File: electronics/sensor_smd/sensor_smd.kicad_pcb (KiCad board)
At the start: 2 copper layers, 40 x 20 mm, 7 parts, among them J1 HEADER MALE RA, U1 HX6286

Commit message: Updates
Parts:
- JP1: moved to B.Cu
- moved JP1 8.40 mm to (129.9, 95.0), turned to 0 degrees
- moved D1 3.50 mm to (131.0, 100.0)
- moved R1 3.00 mm to (128.0, 100.0), turned to 90 degrees
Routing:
- net Net-(R1-Pad2): track 15.8 -> 6.09 mm, vias 0 -> 1
- net VDD: track 20.3 -> 27.9 mm, vias 0 -> 1
- net /SIGNAL: track 14.6 -> 16.8 mm
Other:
- board text added: "↑ Cut to disable LED"
- board text removed: "Cut to disable LED"

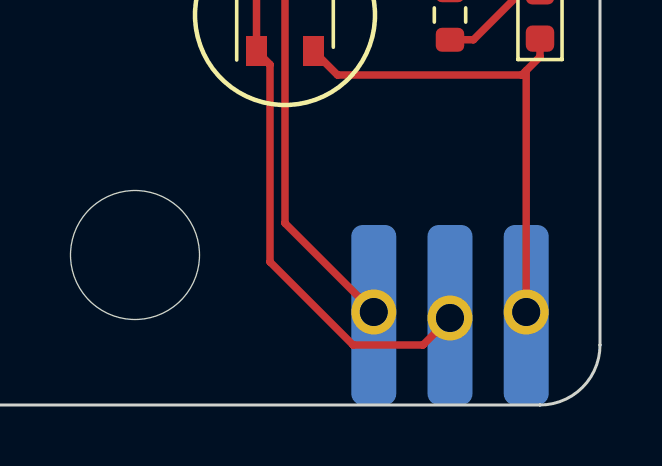
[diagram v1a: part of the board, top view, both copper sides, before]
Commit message: Remove SMD pads from header footprint
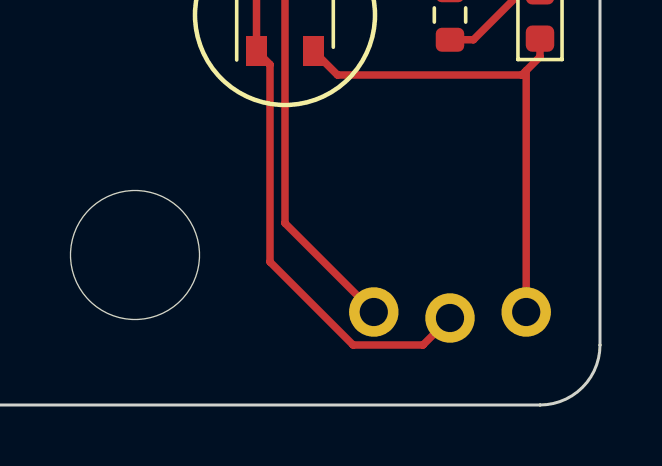
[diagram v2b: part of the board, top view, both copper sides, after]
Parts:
- J1: footprint sensor_smd_lib:header_3_smd -> sensor_smd_lib:header_3
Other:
- board text added: "${COMMIT_HASH} ${COMMIT_DATE}"
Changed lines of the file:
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@@
     )
   )
+  (property "COMMIT_DATE" "YYYY-MM-DD")
+  (property "COMMIT_HASH" "deadbeef")
   (net 0 "")
   (net 1 "/SIGNAL")
@@
     )
   )
-  (footprint "sensor_smd_lib:header_3_smd" (layer "B.Cu")
+  (footprint "sensor_smd_lib:header_3" (layer "B.Cu")
     (at 128 113 180)
     (property "Sheetfile" "sensor_smd.kicad_sch")
     (property "Sheetname" "")
-    (attr smd)
+    (attr through_hole exclude_from_pos_files)
     (fp_text reference "J1" (at 0 0.5 unlocked) (layer "B.SilkS") hide
       (effects (font (size 1 1) (thickness 0.15)) (justify mirror))
@@
       (effects (font (size 1 1) (thickness 0.15)) (justify mirror))
     )
-    (fp_line (start -4 6.5) (end 4 6.5) (layer "B.SilkS") (width 0.12))
-    (fp_line (start 4 6.5) (end 4 0) (layer "B.SilkS") (width 0.12))
-    (fp_line (start -4 0) (end -4 6.5) (layer "B.SilkS") (width 0.12))
+    (fp_line (start 4 4.5) (end 4 0) (layer "B.SilkS") (width 0.12))
+    (fp_line (start -4 0) (end -4 4.5) (layer "B.SilkS") (width 0.12))
+    (fp_line (start -4 4.5) (end 4 4.5) (layer "B.SilkS") (width 0.12))
     (fp_line (start -4 -12) (end 4 -12) (layer "B.Fab") (width 0.1))
     (fp_line (start 4 -12) (end 4 0) (layer "B.Fab") (width 0.1))
     (fp_line (start -4 0) (end -4 -12) (layer "B.Fab") (width 0.1))
-    (pad "1" thru_hole circle (at -2.54 3.1 180) (size 1.5 1.5) (drill 0.94) (layers *.Cu *.Mask)
+    (pad "1" thru_hole circle (at -2.54 3.1 180) (size 1.65 1.65) (drill 0.94) (layers *.Cu *.Mask)
       (net 1 "/SIGNAL") (pinfunction "Pin_1") (pintype "passive"))
-    (pad "1" smd roundrect (at -2.54 3 180) (size 1.5 6) (layers "B.Cu" "B.Paste" "B.Mask") (roundrect_rratio 0.25)
-      (net 1 "/SIGNAL") (pinfunction "Pin_1") (pintype "passive"))
-    (pad "2" thru_hole circle (at 0 2.9 180) (size 1.5 1.5) (drill 0.94) (layers *.Cu *.Mask)
+    (pad "2" thru_hole circle (at 0 2.9 180) (size 1.65 1.65) (drill 0.94) (layers *.Cu *.Mask)
       (net 3 "VDD") (pinfunction "Pin_2") (pintype "passive"))
-    (pad "2" smd roundrect (at 0 3 180) (size 1.5 6) (layers "B.Cu" "B.Paste" "B.Mask") (roundrect_rratio 0.25)
-      (net 3 "VDD") (pinfunction "Pin_2") (pintype "passive"))
-    (pad "3" thru_hole circle (at 2.54 3.1 180) (size 1.5 1.5) (drill 0.94) (layers *.Cu *.Mask)
+    (pad "3" thru_hole circle (at 2.54 3.1 180) (size 1.65 1.65) (drill 0.94) (layers *.Cu *.Mask)
       (net 4 "GND") (pinfunction "Pin_3") (pintype "passive"))
-    (pad "3" smd roundrect (at 2.54 3 180) (size 1.5 6) (layers "B.Cu" "B.Paste" "B.Mask") (roundrect_rratio 0.25)
-      (net 4 "GND") (pinfunction "Pin_3") (pintype "passive"))
-    (model "${KICAD6_3DMODEL_DIR}/Connector_PinHeader_2.54mm.3dshapes/PinHeader_1x03_P2.54mm_Vertical.step"
+    (model "${KICAD6_3DMODEL_DIR}/Connector_PinHeader_2.54mm.3dshapes/PinHeader_1x03_P2.54mm_Vertical.step" hide
       (offset (xyz -2.54 0 0.3))
       (scale (xyz 1 1 1))
       (rotate (xyz -90 90 0))
+    )
+    (model "${KICAD6_3DMODEL_DIR}/Connector_PinHeader_2.54mm.3dshapes/PinHeader_1x03_P2.54mm_Horizontal.step"
+      (offset (xyz 2.54 3 0))
+      (scale (xyz 1 1 1))
+      (rotate (xyz 0 0 90))
     )
   )
@@
   (gr_arc (start 131 93) (mid 132.414214 93.585786) (end 133 95) (layer "Edge.Cuts") (width 0.1))
   (gr_arc (start 95 113) (mid 93.585786 112.414214) (end 93 111) (layer "Edge.Cuts") (width 0.1))
-  (gr_text "S" (at 130.5 105.5) (layer "B.SilkS")
+  (gr_text "S" (at 130.5 107.5) (layer "B.SilkS")
     (effects (font (size 1 1) (thickness 0.15)) (justify mirror))
   )
-  (gr_text "MOTOR" (at 102 109 -10) (layer "B.SilkS")
+  (gr_text "MOTOR" (at 102 107 15) (layer "B.SilkS")
     (effects (font (size 3 3) (thickness 0.3)) (justify mirror))
   )
-  (gr_text "-" (at 125.5 105.5) (layer "B.SilkS")
+  (gr_text "${COMMIT_HASH}\n${COMMIT_DATE}" (at 112.5 110.5) (layer "B.SilkS")
+    (effects (font (size 1 1) (thickness 0.15)) (justify left mirror))
+  )
+  (gr_text "-" (at 125.5 107.5) (layer "B.SilkS")
     (effects (font (size 1 1) (thickness 0.15)) (justify mirror))
   )
-  (gr_text "+" (at 128 105.5) (layer "B.SilkS")
+  (gr_text "+" (at 128 107.5) (layer "B.SilkS")
     (effects (font (size 1 1) (thickness 0.15)) (justify mirror))
   )

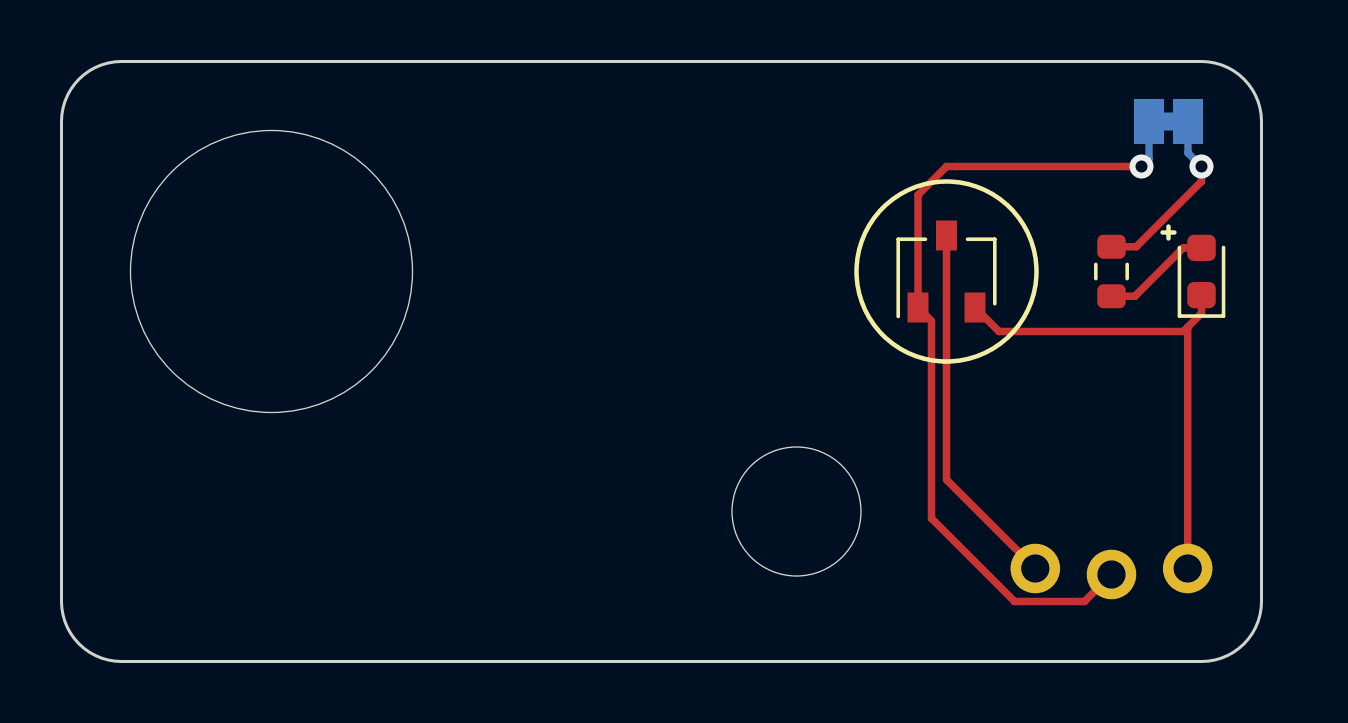
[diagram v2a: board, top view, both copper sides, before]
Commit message: Fix clearance
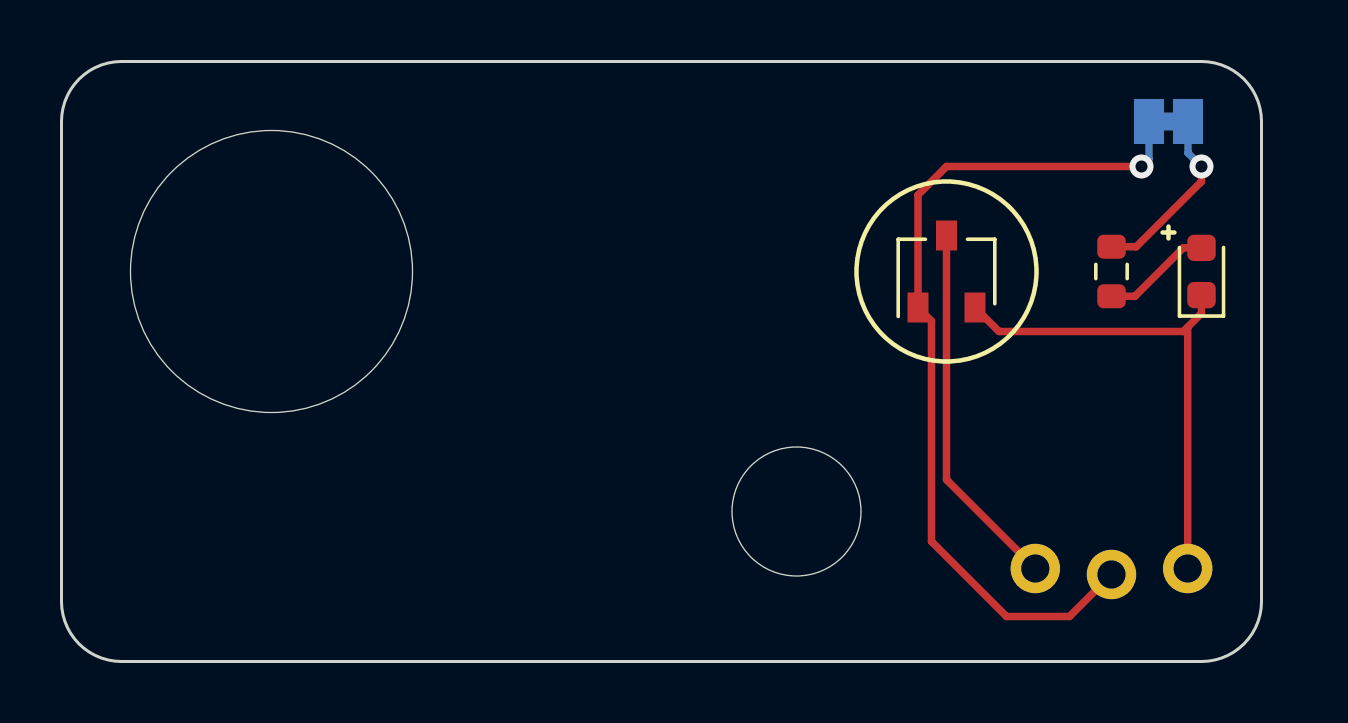
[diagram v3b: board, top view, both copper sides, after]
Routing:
- net VDD: track 27.9 -> 28.8 mm
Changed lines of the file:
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@@
   (segment (start 130.39375 99.2125) (end 131 99.2125) (width 0.25) (layer "F.Cu") (net 2))
   (segment (start 128 100.825) (end 128.78125 100.825) (width 0.25) (layer "F.Cu") (net 2))
-  (segment (start 127.1 111) (end 128 110.1) (width 0.25) (layer "F.Cu") (net 3))
-  (segment (start 122 108.23014) (end 124.76986 111) (width 0.25) (layer "F.Cu") (net 3))
   (segment (start 122.5 96.5) (end 129 96.5) (width 0.25) (layer "F.Cu") (net 3))
+  (segment (start 122 101.65) (end 122 109) (width 0.25) (layer "F.Cu") (net 3))
+  (segment (start 126.6 111.5) (end 128 110.1) (width 0.25) (layer "F.Cu") (net 3))
+  (segment (start 121.55 97.45) (end 122.5 96.5) (width 0.25) (layer "F.Cu") (net 3))
+  (segment (start 124.5 111.5) (end 126.6 111.5) (width 0.25) (layer "F.Cu") (net 3))
+  (segment (start 121.55 101.2) (end 121.55 97.45) (width 0.25) (layer "F.Cu") (net 3))
   (segment (start 121.55 101.2) (end 122 101.65) (width 0.25) (layer "F.Cu") (net 3))
-  (segment (start 122 101.65) (end 122 108.23014) (width 0.25) (layer "F.Cu") (net 3))
-  (segment (start 124.76986 111) (end 127.1 111) (width 0.25) (layer "F.Cu") (net 3))
-  (segment (start 121.55 97.45) (end 122.5 96.5) (width 0.25) (layer "F.Cu") (net 3))
-  (segment (start 121.55 101.2) (end 121.55 97.45) (width 0.25) (layer "F.Cu") (net 3))
+  (segment (start 122 109) (end 124.5 111.5) (width 0.25) (layer "F.Cu") (net 3))
   (via (at 129 96.5) (size 0.8) (drill 0.4) (layers "F.Cu" "B.Cu") (net 3))
   (segment (start 129.25 95) (end 129.25 96.25) (width 0.25) (layer "B.Cu") (net 3))

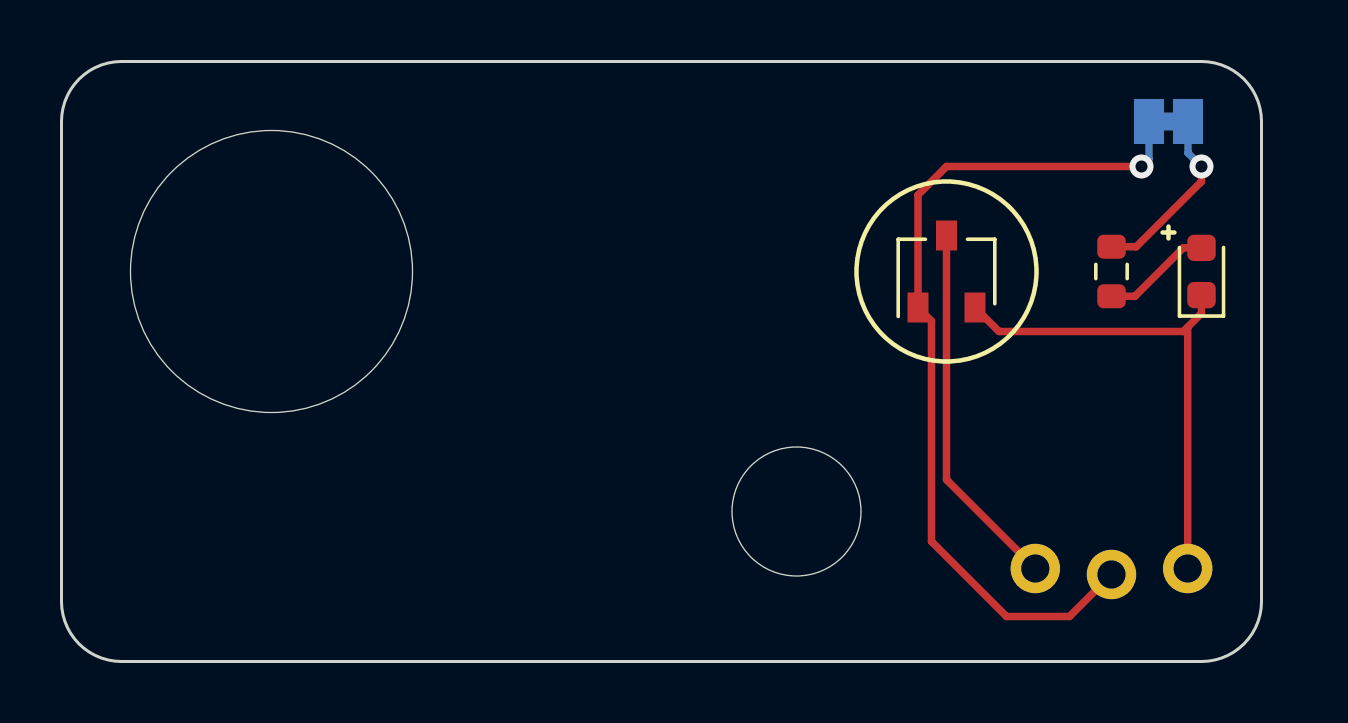
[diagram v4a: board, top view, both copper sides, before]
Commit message: Move sensor inward to support 40-flap spool
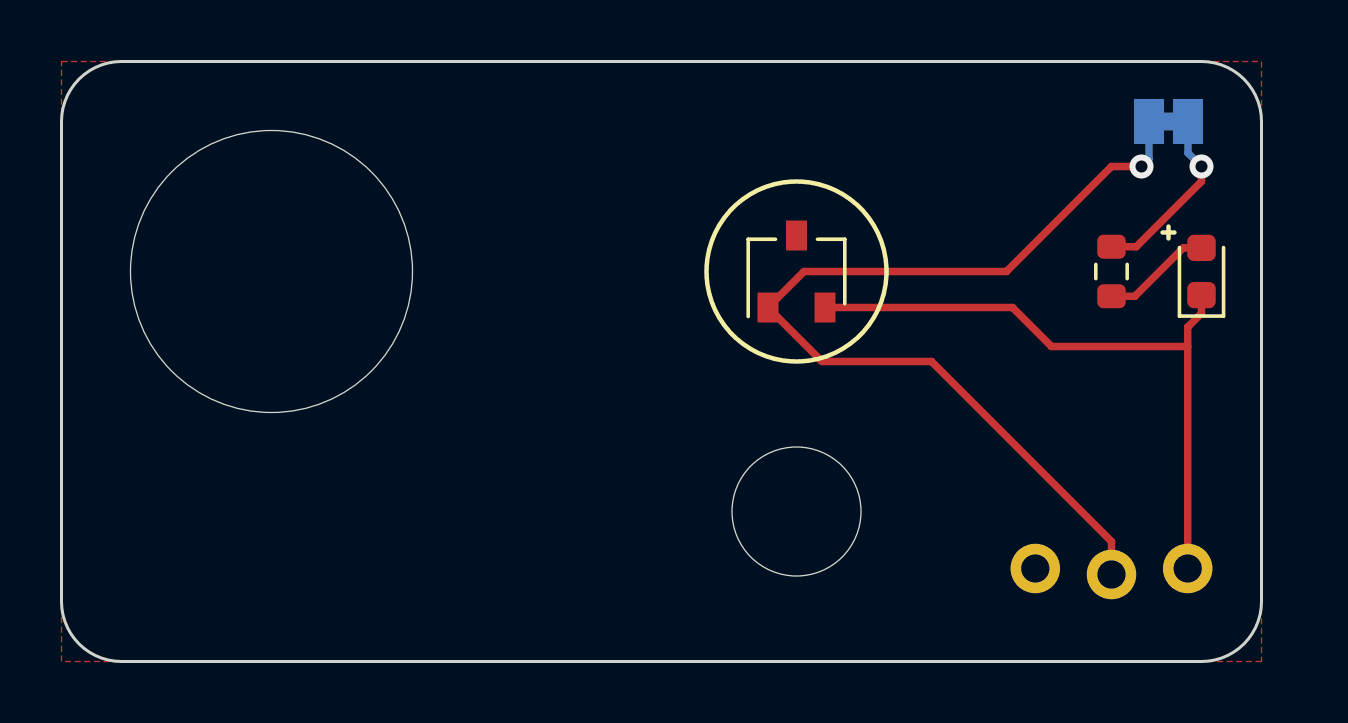
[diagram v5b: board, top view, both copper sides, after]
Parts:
- moved U1 5.00 mm to (117.5, 100.0)
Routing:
- net GND: track 12.3 -> 0.00 mm
- net /SIGNAL: track 16.8 -> 21.9 mm
- net VDD: track 28.8 -> 31.8 mm
- added copper zone on F.Cu, net GND
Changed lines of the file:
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@@
   )
   (footprint "Package_TO_SOT_SMD:SOT-23W" (layer "F.Cu")
-    (at 122.5 100 90)
+    (at 117.5 100 90)
     (descr "SOT-23W http://www.allegromicro.com/~/media/Files/Datasheets/A112x-Datasheet.ashx?la=en&hash=7BC461E058CC246E0BAB62433B2F1ECA104CA9D3")
     (tags "SOT-23W")
@@
   (gr_line (start 129.9 98.5) (end 129.9 98.9) (layer "F.SilkS") (width 0.15))
   (gr_line (start 130.1 98.7) (end 129.7 98.7) (layer "F.SilkS") (width 0.15))
-  (gr_circle (center 122.5 100) (end 125.5 100) (layer "F.SilkS") (width 0.15) (fill none))
+  (gr_circle (center 117.5 100) (end 120.5 100) (layer "F.SilkS") (width 0.15) (fill none))
   (gr_arc (start 93 95) (mid 93.585786 93.585786) (end 95 93) (layer "Edge.Cuts") (width 0.1))
   (gr_arc (start 133 111) (mid 132.414214 112.414214) (end 131 113) (layer "Edge.Cuts") (width 0.1))
@@
   )
   (dimension (type aligned) (layer "Cmts.User")
-    (pts (xy 117.5 100) (xy 122.5 100))
-    (height -10)
-    (gr_text "5.0000 mm" (at 120 88.85) (layer "Cmts.User")
-      (effects (font (size 1 1) (thickness 0.15)))
-    )
-    (format (units 3) (units_format 1) (precision 4))
-    (style (thickness 0.15) (arrow_length 1.27) (text_position_mode 0) (extension_height 0.58642) (extension_offset 0.5) keep_text_aligned)
-  )
-  (dimension (type aligned) (layer "Cmts.User")
     (pts (xy 128 110) (xy 128 100))
     (height 10)
@@
   (segment (start 131 100.7875) (end 131 101.39375) (width 0.25) (layer "F.Cu") (net 1))
   (segment (start 130.54 101.85375) (end 130.54 109.9) (width 0.25) (layer "F.Cu") (net 1))
-  (segment (start 130.39375 102) (end 130.54 101.85375) (width 0.25) (layer "F.Cu") (net 1))
-  (segment (start 124.25 102) (end 130.39375 102) (width 0.25) (layer "F.Cu") (net 1))
+  (segment (start 124.7 101.2) (end 126 102.5) (width 0.25) (layer "F.Cu") (net 1))
+  (segment (start 118.45 101.2) (end 124.7 101.2) (width 0.25) (layer "F.Cu") (net 1))
   (segment (start 131 101.39375) (end 130.54 101.85375) (width 0.25) (layer "F.Cu") (net 1))
-  (segment (start 123.45 101.2) (end 124.25 102) (width 0.25) (layer "F.Cu") (net 1))
+  (segment (start 126 102.5) (end 130.54 102.5) (width 0.25) (layer "F.Cu") (net 1))
   (segment (start 128.78125 100.825) (end 130.39375 99.2125) (width 0.25) (layer "F.Cu") (net 2))
   (segment (start 130.39375 99.2125) (end 131 99.2125) (width 0.25) (layer "F.Cu") (net 2))
   (segment (start 128 100.825) (end 128.78125 100.825) (width 0.25) (layer "F.Cu") (net 2))
-  (segment (start 122.5 96.5) (end 129 96.5) (width 0.25) (layer "F.Cu") (net 3))
-  (segment (start 122 101.65) (end 122 109) (width 0.25) (layer "F.Cu") (net 3))
-  (segment (start 126.6 111.5) (end 128 110.1) (width 0.25) (layer "F.Cu") (net 3))
-  (segment (start 121.55 97.45) (end 122.5 96.5) (width 0.25) (layer "F.Cu") (net 3))
-  (segment (start 124.5 111.5) (end 126.6 111.5) (width 0.25) (layer "F.Cu") (net 3))
-  (segment (start 121.55 101.2) (end 121.55 97.45) (width 0.25) (layer "F.Cu") (net 3))
-  (segment (start 121.55 101.2) (end 122 101.65) (width 0.25) (layer "F.Cu") (net 3))
-  (segment (start 122 109) (end 124.5 111.5) (width 0.25) (layer "F.Cu") (net 3))
+  (segment (start 116.55 101.2) (end 117.75 100) (width 0.25) (layer "F.Cu") (net 3))
+  (segment (start 128 109) (end 128 110.1) (width 0.25) (layer "F.Cu") (net 3))
+  (segment (start 118.35 103) (end 122 103) (width 0.25) (layer "F.Cu") (net 3))
+  (segment (start 122 103) (end 128 109) (width 0.25) (layer "F.Cu") (net 3))
+  (segment (start 128 96.5) (end 129 96.5) (width 0.25) (layer "F.Cu") (net 3))
+  (segment (start 117.75 100) (end 124.5 100) (width 0.25) (layer "F.Cu") (net 3))
+  (segment (start 124.5 100) (end 128 96.5) (width 0.25) (layer "F.Cu") (net 3))
+  (segment (start 116.55 101.2) (end 118.35 103) (width 0.25) (layer "F.Cu") (net 3))
   (via (at 129 96.5) (size 0.8) (drill 0.4) (layers "F.Cu" "B.Cu") (net 3))
   (segment (start 129.25 95) (end 129.25 96.25) (width 0.25) (layer "B.Cu") (net 3))
   (segment (start 129.25 96.25) (end 129 96.5) (width 0.25) (layer "B.Cu") (net 3))
-  (segment (start 122.5 106.94) (end 125.46 109.9) (width 0.25) (layer "F.Cu") (net 4))
-  (segment (start 122.5 98.8) (end 122.5 106.94) (width 0.25) (layer "F.Cu") (net 4))
   (segment (start 128 99.175) (end 128.825 99.175) (width 0.25) (layer "F.Cu") (net 5))
   (segment (start 128.825 99.175) (end 131 97) (width 0.25) (layer "F.Cu") (net 5))
@@
   (segment (start 130.55 95) (end 130.55 96.05) (width 0.25) (layer "B.Cu") (net 5))
   (segment (start 130.55 96.05) (end 131 96.5) (width 0.25) (layer "B.Cu") (net 5))
+  (zone (net 4) (net_name "GND") (layer "F.Cu") (hatch edge 0.508)
+    (connect_pads (clearance 0.254))
+    (min_thickness 0.254) (filled_areas_thickness no)
+    (fill yes (thermal_gap 0.508) (thermal_bridge_width 0.508))
+    (polygon
+      (pts
+        (xy 133 113)
+        (xy 93 113)
+        (xy 93 93)
+        (xy 133 93)
+      )
+    )
+  )
 )

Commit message: More readme updates
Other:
- board text added: "Splitflap Sensor"
- board text added: "v2.0"
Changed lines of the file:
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@@
     (effects (font (size 1 1) (thickness 0.15)) (justify mirror))
+  )
+  (gr_text "Splitflap Sensor" (at 94 110) (layer "F.SilkS")
+    (effects (font (size 1 1) (thickness 0.15) italic) (justify left))
+  )
+  (gr_text "v2.0" (at 94 111.5) (layer "F.SilkS")
+    (effects (font (size 0.8 0.8) (thickness 0.1) italic) (justify left))
   )
   (dimension (type aligned) (layer "Cmts.User")
